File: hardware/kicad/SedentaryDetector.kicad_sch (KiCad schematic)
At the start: 2 parts, among them J1 ESP32-WROOM-32, J2 MPU6050-GY521

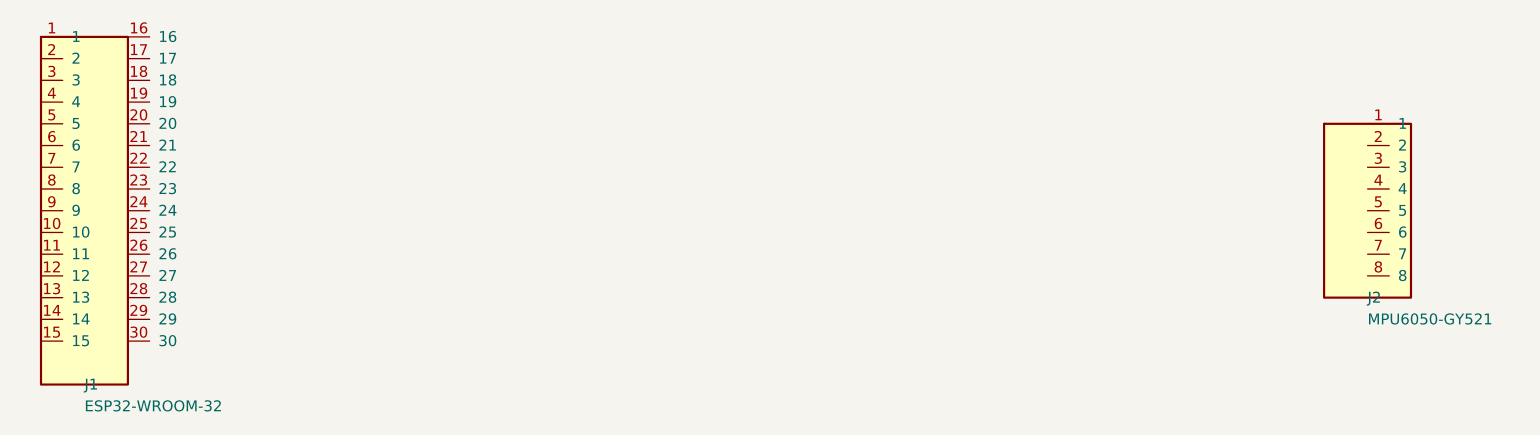
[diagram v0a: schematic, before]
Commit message: fix(schematic): create matching schematic for J1(2x15) J2(1x8)
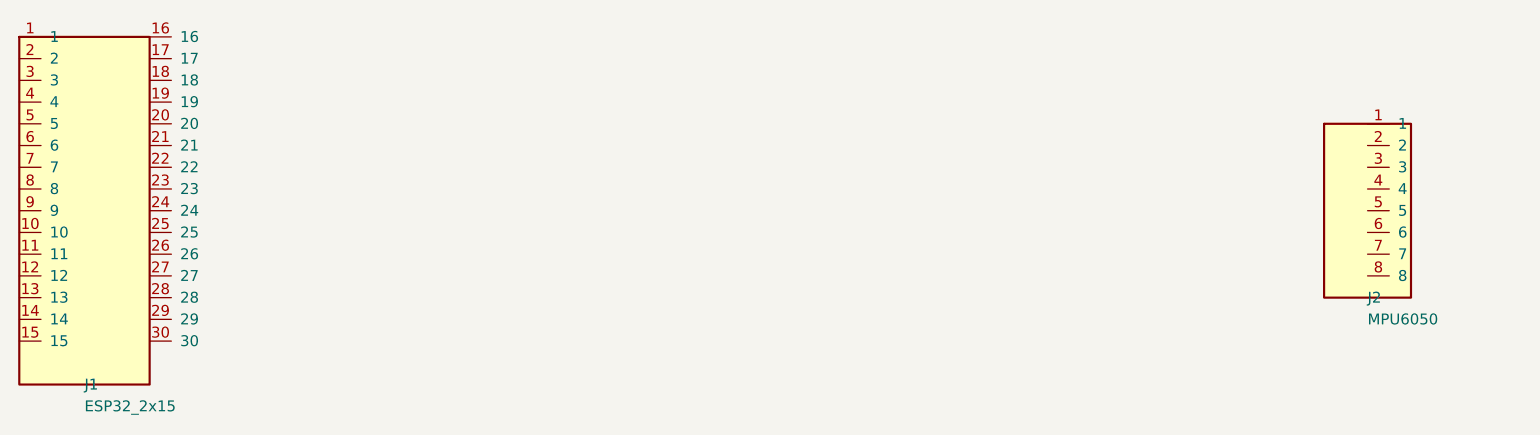
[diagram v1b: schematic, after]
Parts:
- J1: value ESP32-WROOM-32 -> ESP32_2x15; footprint Connector_PinSocket_2.54mm:PinSocket_2x15_P2.54mm_Vertical -> (none)
- J2: value MPU6050-GY521 -> MPU6050; footprint Connector_PinSocket_2.54mm:PinSocket_1x08_P2.54mm_Vertical -> (none)
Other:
- company: Personal Project -> (none)
- title: Sedentary Detector - Carrier Board -> Sedentary Detector
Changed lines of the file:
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@@
 (kicad_sch (version 20250114) (generator "eeschema")
 	(paper "A3")
-	(title_block
-		(title "Sedentary Detector - Carrier Board")
-		(date "2026-06-20")
-		(rev "0.1")
-		(company "Personal Project")
-	)
+	(title_block (title "Sedentary Detector") (date "2026-06-20") (rev "0.2"))
 	(symbol (lib_id "Conn_02x15") (at 50 100 0) (unit 1) (in_bom yes) (on_board yes)
-		(property "Reference" "J1" (at 50 120.32 0)
-			(effects (font (size 1.27 1.27)) (justify left))
-		)
-		(property "Value" "ESP32-WROOM-32" (at 50 122.86 0)
-			(effects (font (size 1.27 1.27)) (justify left))
-		)
-		(property "Footprint" "Connector_PinSocket_2.54mm:PinSocket_2x15_P2.54mm_Vertical" (at 50 80 0)
-			(effects (font (size 1.27 1.27)) (hide yes))
-		)
-		(property "Datasheet" "~" (at 50 80 0)
-			(effects (font (size 1.27 1.27)) (hide yes))
-		)
+		(property "Reference" "J1" (at 50 120.32 0) (effects (font (size 1.27 1.27)) (justify left)))
+		(property "Value" "ESP32_2x15" (at 50 122.86 0) (effects (font (size 1.27 1.27)) (justify left)))
+		(property "Footprint" "" (at 50 80 0) (effects (font (size 1.27 1.27)) (hide yes)))
+		(property "Datasheet" "~" (at 50 80 0) (effects (font (size 1.27 1.27)) (hide yes)))
 		(pin "1")
 		(pin "2")
@@
 	)
 	(symbol (lib_id "Conn_01x08") (at 200 100 0) (unit 1) (in_bom yes) (on_board yes)
-		(property "Reference" "J2" (at 200 110.16 0)
-			(effects (font (size 1.27 1.27)) (justify left))
-		)
-		(property "Value" "MPU6050-GY521" (at 200 112.7 0)
-			(effects (font (size 1.27 1.27)) (justify left))
-		)
-		(property "Footprint" "Connector_PinSocket_2.54mm:PinSocket_1x08_P2.54mm_Vertical" (at 200 90 0)
-			(effects (font (size 1.27 1.27)) (hide yes))
-		)
-		(property "Datasheet" "~" (at 200 90 0)
-			(effects (font (size 1.27 1.27)) (hide yes))
-		)
+		(property "Reference" "J2" (at 200 110.16 0) (effects (font (size 1.27 1.27)) (justify left)))
+		(property "Value" "MPU6050" (at 200 112.7 0) (effects (font (size 1.27 1.27)) (justify left)))
+		(property "Footprint" "" (at 200 90 0) (effects (font (size 1.27 1.27)) (hide yes)))
+		(property "Datasheet" "~" (at 200 90 0) (effects (font (size 1.27 1.27)) (hide yes)))
 		(pin "1")
 		(pin "2")
@@
 		(pin "8")
 	)
-	(sheet_instances
-		(path "/" (page "1"))
-	)
+	(sheet_instances (path "/" (page "1")))
 )

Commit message: fix(hardware): assign nets, GND pour - user to route
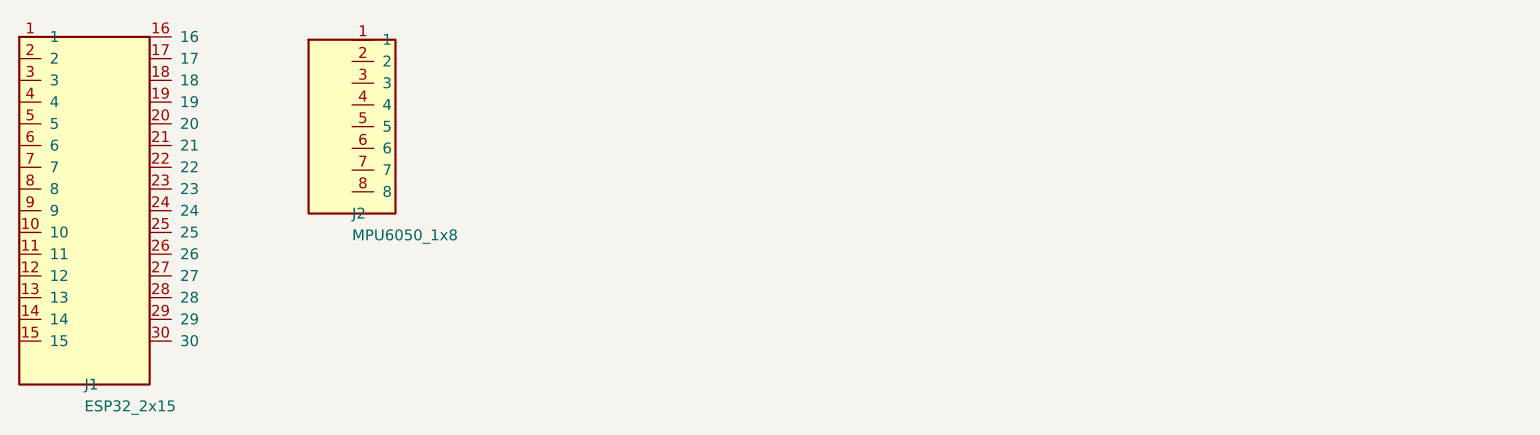
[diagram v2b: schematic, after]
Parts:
- J2: value MPU6050 -> MPU6050_1x8
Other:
- moved on the sheet: J2
